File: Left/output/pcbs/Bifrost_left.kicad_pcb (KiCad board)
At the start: 2 copper layers, 145.4 x 130.3 mm, 66 parts

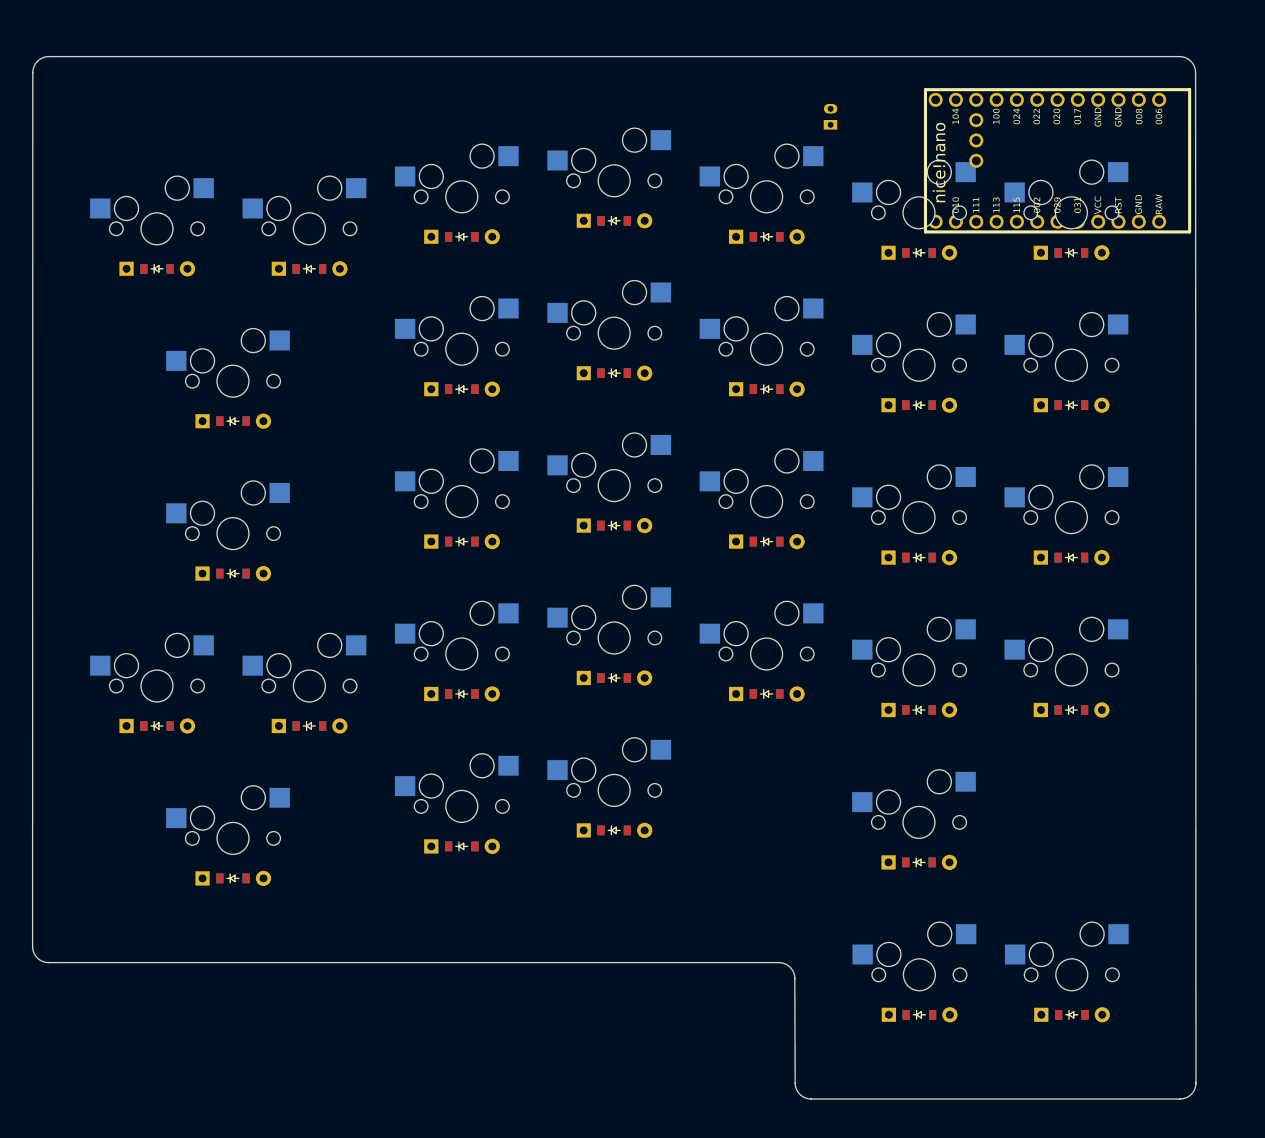
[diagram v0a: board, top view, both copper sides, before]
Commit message: finish left PCB layout. Needs wires and stabs
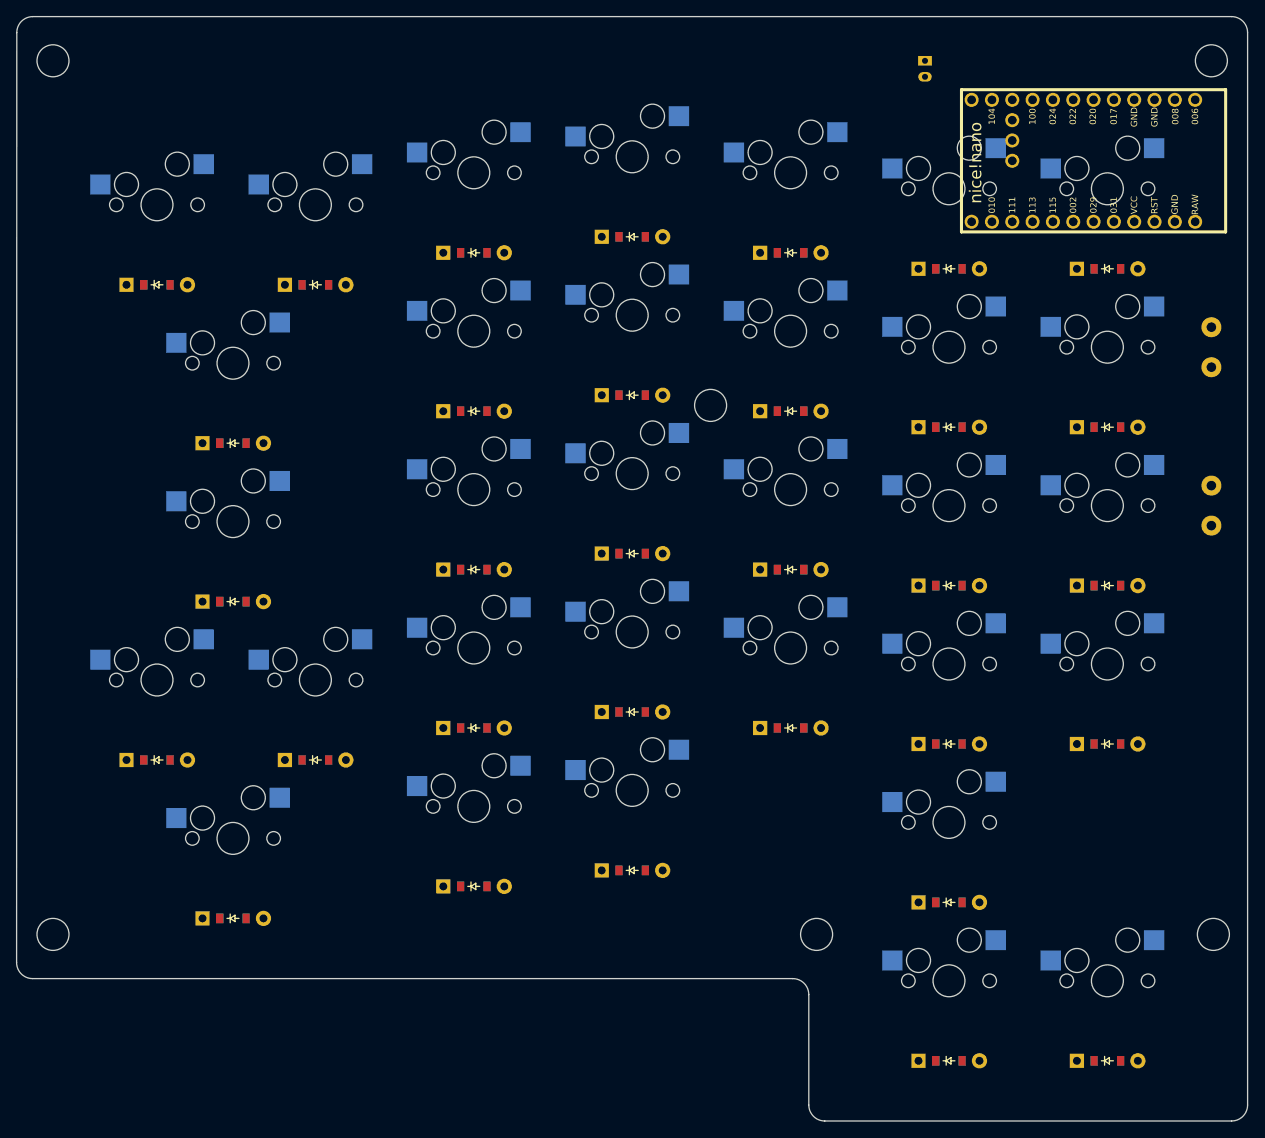
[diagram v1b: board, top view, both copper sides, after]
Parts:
- added ?: , HOLE_M2_TH, F.Cu at (87.0, 102.8)
- added ?: , HOLE_M2_TH, F.Cu at (231.8, 102.8)
- added ?: , HOLE_M2_TH, F.Cu at (87.0, 212.0)
- added ?: , HOLE_M2_TH, F.Cu at (232.1, 212.0)
- added ?: , HOLE_M2_TH, F.Cu at (169.2, 145.9)
- added ?: , HOLE_M2_TH, F.Cu at (182.5, 212.0)
- added SW1: , switch_tht, F.Cu at (231.8, 138.6)
- added SW2: , switch_tht, F.Cu at (231.8, 158.4)
- moved JST1 13.2 mm to (196.0, 103.8), turned to 270 degrees
- moved D32 7.27 mm to (218.8, 227.8)
- moved D31 6.84 mm to (199.0, 227.8)
- moved D22 6.25 mm to (199.0, 208.0)
- moved D27 6.19 mm to (218.8, 188.2)
- moved D28 5.70 mm to (218.8, 168.4)
- moved D23 5.67 mm to (199.0, 188.2)
- moved D13 5.48 mm to (159.4, 204.0)
- moved S30 5.41 mm to (218.8, 118.8)
- moved D29 5.27 mm to (218.8, 148.6)
- moved D8 5.22 mm to (139.6, 206.0)
- moved D18 5.20 mm to (179.2, 186.2)
- moved D24 5.13 mm to (199.0, 168.4)
- moved S29 5.03 mm to (218.8, 138.6)
- moved D1 5.00 mm to (109.5, 210.0)
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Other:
- board size 145.4 x 130.3 mm -> 153.9 x 138.1 mm

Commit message: finish left?
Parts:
- removed the ? at (87.0, 102.8)
- removed the ? at (231.8, 102.8)
- removed the ? at (169.2, 145.9)
- removed the ? at (182.5, 212.0)
- added ?: , HOLE_M2_TH, F.Cu at (182.4, 212.0)
- added ?: , HOLE_M2_TH, F.Cu at (231.8, 102.8)
- added ?: , HOLE_M2_TH, F.Cu at (169.2, 145.9)
- added ?: , HOLE_M2_TH, F.Cu at (87.0, 102.8)
- moved SW2 69.4 mm to (189.0, 103.8)
- moved SW1 61.5 mm to (182.5, 101.8)
- moved JST1 19.8 mm to (176.2, 103.8)
- moved MCU1 2.73 mm to (218.5, 115.3)
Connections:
- D31 pad 1: P009 -> P002
- D32 pad 1: P009 -> P002
- S1 pad 1: P106 -> P024
- S13 pad 1: P100 -> P104
- S14 pad 1: P100 -> P104
- S15 pad 1: P100 -> P104
- S16 pad 1: P100 -> P104
- S17 pad 1: P100 -> P104
- S18 pad 1: P024 -> P106
- S19 pad 1: P024 -> P106
- S2 pad 1: P106 -> P024
- S20 pad 1: P024 -> P106
- S21 pad 1: P024 -> P106
- S3 pad 1: P106 -> P024
- S31 pad 1: P024 -> P022
- S4 pad 1: P106 -> P024
- S5 pad 1: P106 -> P024
- S6 pad 1: P104 -> P100
- S7 pad 1: P104 -> P100
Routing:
- net P024: track 0.00 -> 243.9 mm
- net P115: track 0.00 -> 230.3 mm
- net P113: track 0.00 -> 228.0 mm
- net P111: track 0.00 -> 194.3 mm
- net P010: track 0.00 -> 184.5 mm
- net P100: track 0.00 -> 172.2 mm
- net P011: track 0.00 -> 162.2 mm
- net P009: track 0.00 -> 147.6 mm
- net P002: track 0.00 -> 145.5 mm
- net P104: track 0.00 -> 136.9 mm
- net P022: track 0.00 -> 127.9 mm
- net P020: track 0.00 -> 111.5 mm
- net P106: track 0.00 -> 94.6 mm
- net RAW: track 0.00 -> 68.0 mm
- net RST: track 0.00 -> 56.7 mm
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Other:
- board size 153.9 x 138.1 mm -> 153.9 x 138 mm
- net class Default removed

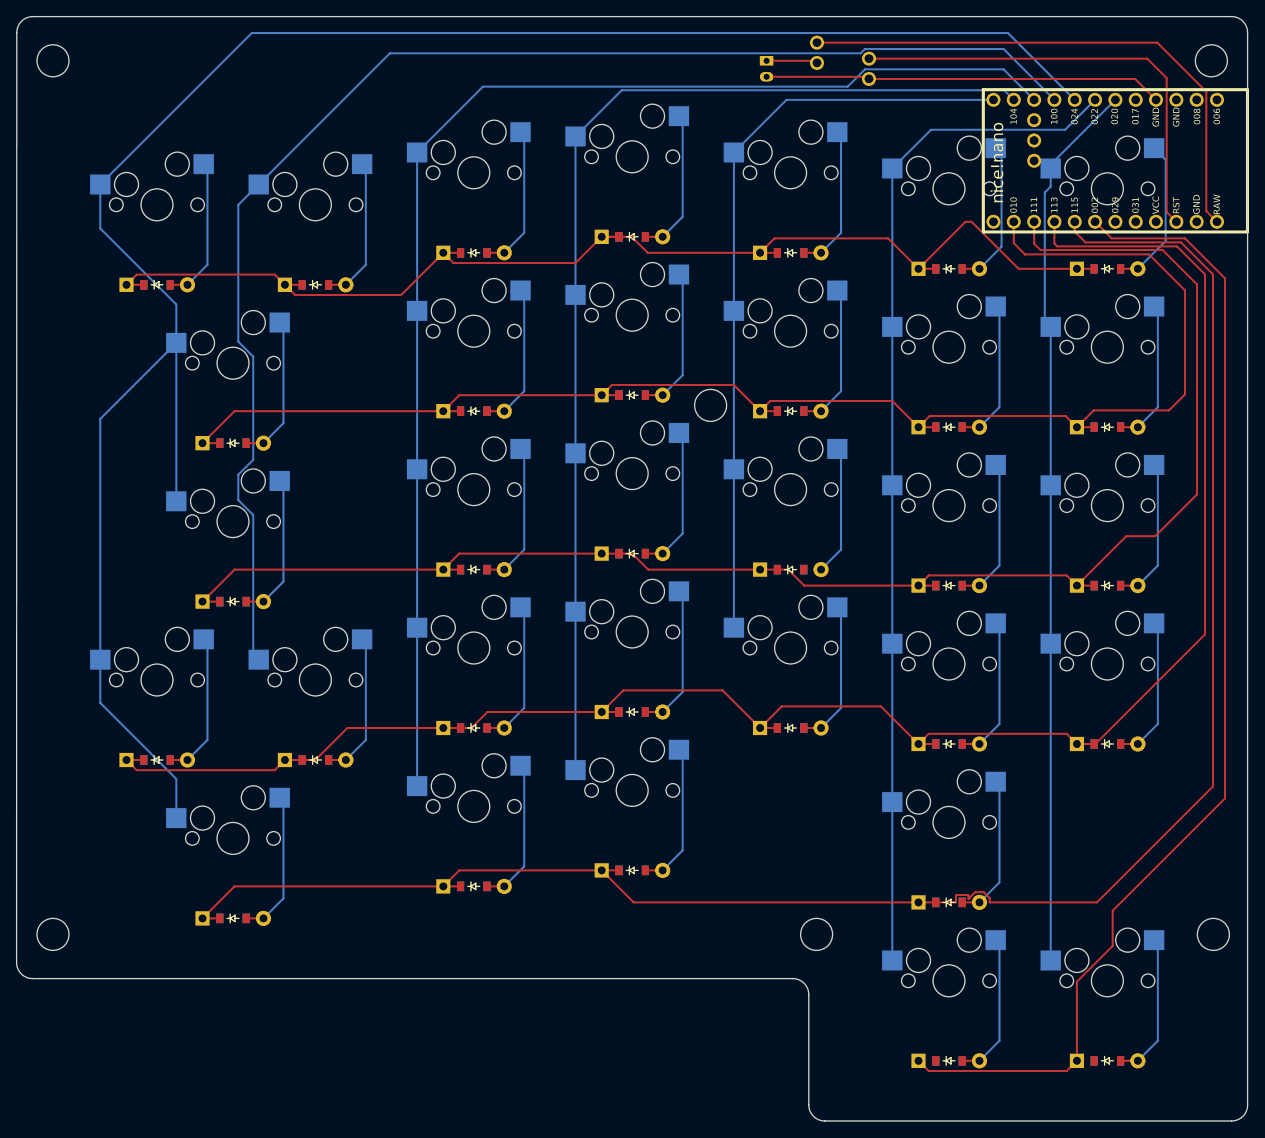
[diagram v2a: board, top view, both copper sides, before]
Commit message: added stabs to left
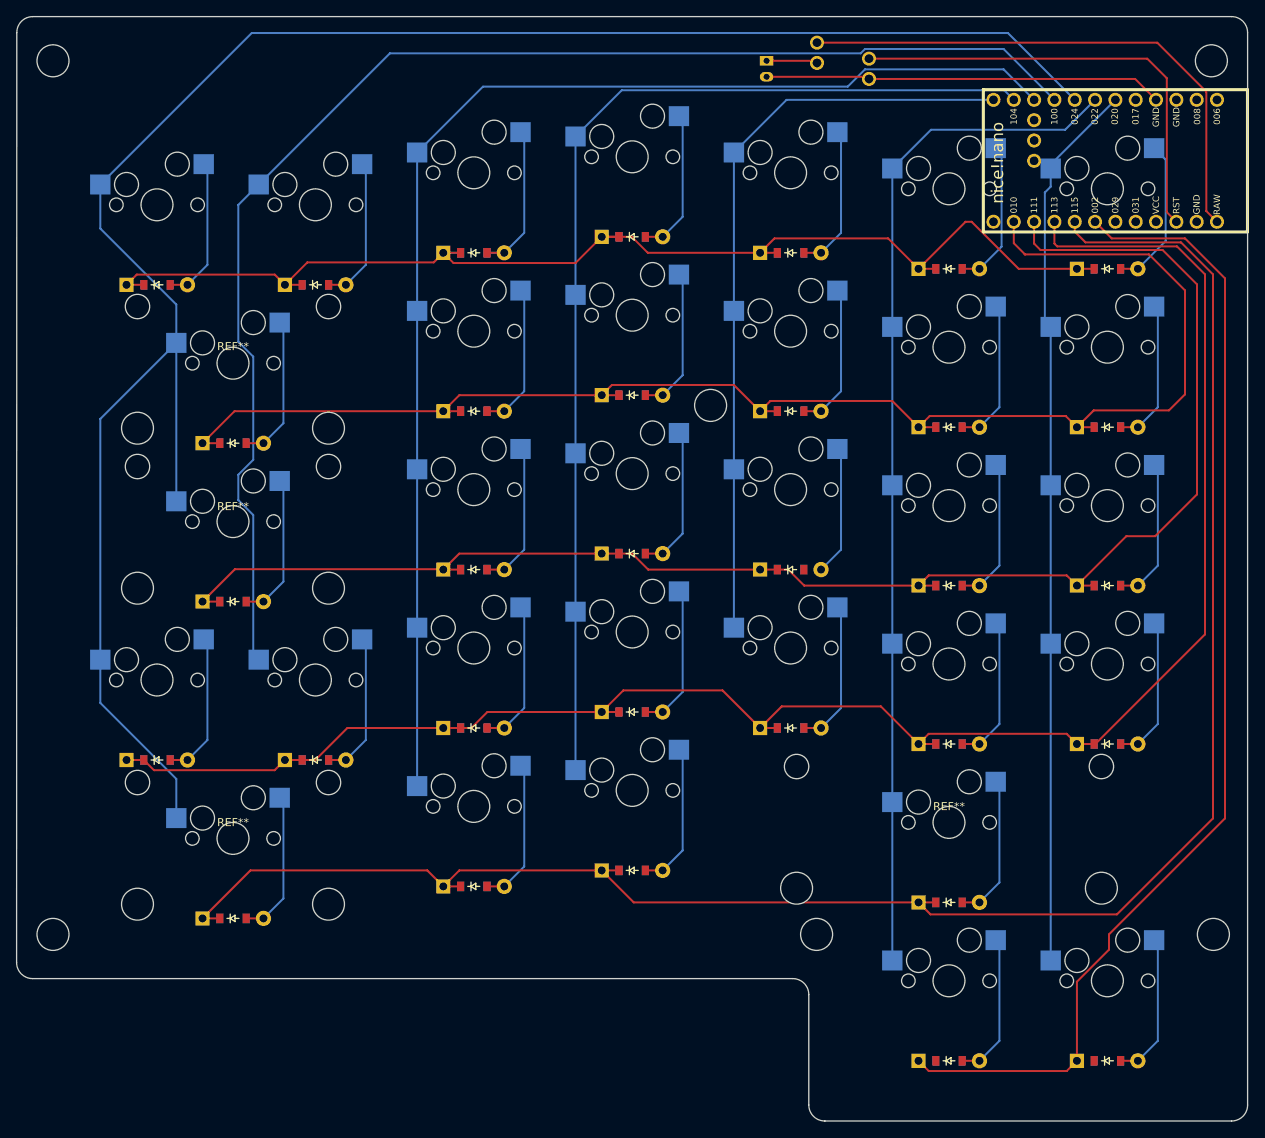
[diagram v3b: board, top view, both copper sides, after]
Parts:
- added REF**: Stabilizer_Cherry_MX_2.00u, PCM_Mounting_Keyboard_Stabilizer:Stabilizer_Cherry_MX_2.00u, F.Cu at (109.5, 200.0)
- added REF**: Stabilizer_Cherry_MX_2.00u, PCM_Mounting_Keyboard_Stabilizer:Stabilizer_Cherry_MX_2.00u, F.Cu at (109.5, 160.5)
- added REF**: Stabilizer_Cherry_MX_3.00u, PCM_Mounting_Keyboard_Stabilizer:Stabilizer_Cherry_MX_3.00u, F.Cu at (199.0, 198.0)
- added REF**: Stabilizer_Cherry_MX_2.00u, PCM_Mounting_Keyboard_Stabilizer:Stabilizer_Cherry_MX_2.00u, F.Cu at (109.5, 140.5)
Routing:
- net P115: track 230.3 -> 235.1 mm
- net c3_r1: track 18.5 -> 20.6 mm
- net P113: track 228.0 -> 225.8 mm
- net P009: track 147.6 -> 148.7 mm

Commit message: update
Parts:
- moved REF** 0.10 mm to (109.5, 160.4)
- moved REF** 0.10 mm to (109.5, 140.4)
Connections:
- MCU1 pad 33: P107 -> (no net)
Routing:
- net P113: track 225.8 -> 241.0 mm
- net P009: track 148.7 -> 163.3 mm
- net P010: track 184.5 -> 197.7 mm
- net P111: track 194.4 -> 207.4 mm
- net P115: track 235.1 -> 244.5 mm
- net P002: track 145.5 -> 154.1 mm
- net c5_r3: track 16.3 -> 20.6 mm
- net c6_r1: track 18.7 -> 21.0 mm
- net space_cluster: track 18.5 -> 20.6 mm
- net c7_r3: track 18.5 -> 20.6 mm
- net c7_r2: track 18.5 -> 20.6 mm
- net c7_r1: track 19.3 -> 21.4 mm
- net c7_r4: track 18.5 -> 20.6 mm
- net layer_cluster: track 18.5 -> 20.6 mm
- net c6_r5: track 18.5 -> 20.6 mm
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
